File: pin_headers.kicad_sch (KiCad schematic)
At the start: 0 parts

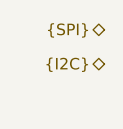
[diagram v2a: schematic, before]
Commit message: Follow DC-DC typical application
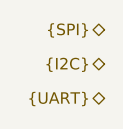
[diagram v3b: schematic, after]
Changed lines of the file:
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@@
 		(rev "1.0")
+	)
+	(hierarchical_label "{UART}"
+		(shape bidirectional)
+		(at 109.22 88.9 180)
+		(effects
+			(font
+				(size 1.27 1.27)
+			)
+			(justify right)
+		)
 	)
 	(hierarchical_label "{SPI}"

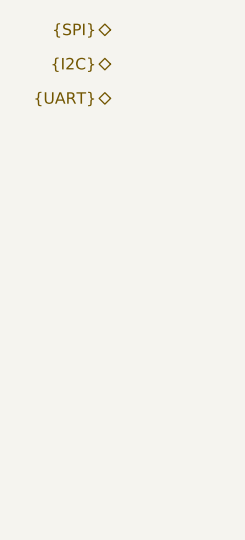
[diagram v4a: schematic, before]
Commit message: Reset PCB and lock mounting holes
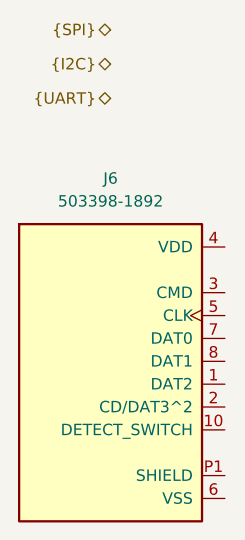
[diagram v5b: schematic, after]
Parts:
- added J6: 503398-1892, Tumbler2:MOLEX_503398-1892, symbol Tumbler2:503398-1892
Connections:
- new net: J6.P1 (SHIELD), J6.P2 (SHIELD), J6.P3 (SHIELD), J6.P4 (SHIELD)
- new net VSS: J6.6 (VSS), J6.9 (VSS)
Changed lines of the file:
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@@
+		)
+	)
+	(symbol
+		(lib_id "Tumbler2:503398-1892")
+		(at 109.22 119.38 0)
+		(unit 1)
+		(exclude_from_sim no)
+		(in_bom yes)
+		(on_board yes)
+		(dnp no)
+		(fields_autoplaced yes)
+		(property "Reference" "J6"
+			(at 109.22 97.79 0)
+			(effects
+				(font
+					(size 1.27 1.27)
+				)
+			)
+		)
+		(property "Value" "503398-1892"
+			(at 109.22 100.33 0)
+			(effects
+				(font
+					(size 1.27 1.27)
+				)
+			)
+		)
+		(property "Footprint" "Tumbler2:MOLEX_503398-1892"
+			(at 109.22 119.38 0)
+			(effects
+				(font
+					(size 1.27 1.27)
+				)
+				(justify bottom)
+				(hide yes)
+			)
+		)
+		(property "Datasheet" "https://www.molex.com/en-us/products/part-detail/5033981892?display=pdf"
+			(at 109.22 119.38 0)
+			(effects
+				(font
+					(size 1.27 1.27)
+				)
+				(hide yes)
+			)
+		)
+		(property "Description" "Micro SD card (TF card) Connector and Ejector Push-Push Surface Mount"
+			(at 109.22 119.38 0)
+			(effects
+				(font
+					(size 1.27 1.27)
+				)
+				(hide yes)
+			)
+		)
+		(property "LSCS Part Nr." "C428492"
+			(at 109.22 119.38 0)
+			(effects
+				(font
+					(size 1.27 1.27)
+				)
+				(hide yes)
+			)
+		)
+		(property "SnapEDA_Link" "https://www.snapeda.com/parts/503398-1892/Molex/view-part/?ref=snap"
+			(at 109.22 119.38 0)
+			(effects
+				(font
+					(size 1.27 1.27)
+				)
+				(justify bottom)
+				(hide yes)
+			)
+		)
+		(pin "4"
+		)
+		(pin "3"
+		)
+		(pin "5"
+		)
+		(pin "7"
+		)
+		(pin "8"
+		)
+		(pin "P2"
+		)
+		(pin "P4"
+		)
+		(pin "9"
+		)
+		(pin "P3"
+		)
+		(pin "10"
+		)
+		(pin "P1"
+		)
+		(pin "6"
+		)
+		(pin "1"
+		)
+		(pin "2"
+		)
+		(instances
+			(project ""
+				(path "/f3fd8d79-9d35-4c04-811e-2697a2740958/13a39940-d4ea-453b-93b0-cf8a2a454837"
+					(reference "J6")
+					(unit 1)
+				)
+			)
 		)
 	)

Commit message: Update LCSC symbol field
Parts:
- J6: LCSC Part (none) -> C428492; LSCS Part Nr. C428492 -> (none)
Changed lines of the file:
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@@
-			)
-		)
-		(property "LSCS Part Nr." "C428492"
-			(at 109.22 119.38 0)
-			(effects
-				(font
-					(size 1.27 1.27)
-				)
-				(hide yes)
 			)
 		)
@@
 				(hide yes)
 			)
+		)
+		(property "LCSC Part" "C428492"
+			(at 109.22 119.38 0)
+			(effects
+				(font
+					(size 1.27 1.27)
+				)
+				(hide yes)
+			)

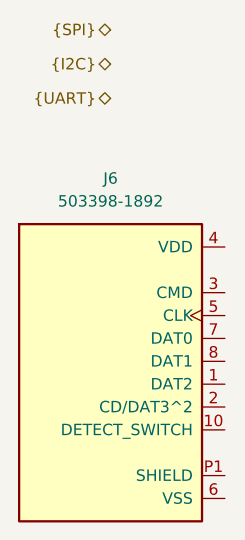
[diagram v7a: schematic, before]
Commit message: Undo component replacement
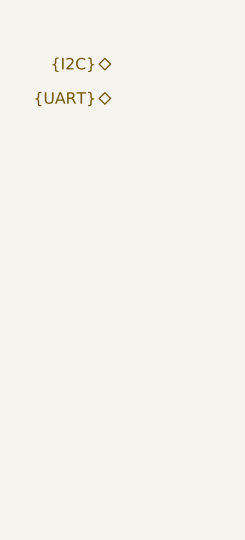
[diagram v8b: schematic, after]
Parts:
- removed J6: 503398-1892, Tumbler2:MOLEX_503398-1892, symbol Tumbler2:503398-1892
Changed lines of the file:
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@@
-		)
-	)
-	(hierarchical_label "{SPI}"
-		(shape bidirectional)
-		(at 109.22 81.28 180)
-		(effects
-			(font
-				(size 1.27 1.27)
-			)
-			(justify right)
 		)
 	)
@@
 		)
 	)
-	(symbol
-		(lib_id "Tumbler2:503398-1892")
-		(at 109.22 119.38 0)
-		(unit 1)
-		(exclude_from_sim no)
-		(in_bom yes)
-		(on_board yes)
-		(dnp no)
-		(fields_autoplaced yes)
-		(property "Reference" "J6"
-			(at 109.22 97.79 0)
-			(effects
-				(font
-					(size 1.27 1.27)
-				)
-			)
-		)
-		(property "Value" "503398-1892"
-			(at 109.22 100.33 0)
-			(effects
-				(font
-					(size 1.27 1.27)
-				)
-			)
-		)
-		(property "Footprint" "Tumbler2:MOLEX_503398-1892"
-			(at 109.22 119.38 0)
-			(effects
-				(font
-					(size 1.27 1.27)
-				)
-				(justify bottom)
-				(hide yes)
-			)
-		)
-		(property "Datasheet" "https://www.molex.com/en-us/products/part-detail/5033981892?display=pdf"
-			(at 109.22 119.38 0)
-			(effects
-				(font
-					(size 1.27 1.27)
-				)
-				(hide yes)
-			)
-		)
-		(property "Description" "Micro SD card (TF card) Connector and Ejector Push-Push Surface Mount"
-			(at 109.22 119.38 0)
-			(effects
-				(font
-					(size 1.27 1.27)
-				)
-				(hide yes)
-			)
-		)
-		(property "SnapEDA_Link" "https://www.snapeda.com/parts/503398-1892/Molex/view-part/?ref=snap"
-			(at 109.22 119.38 0)
-			(effects
-				(font
-					(size 1.27 1.27)
-				)
-				(justify bottom)
-				(hide yes)
-			)
-		)
-		(property "LCSC Part" "C428492"
-			(at 109.22 119.38 0)
-			(effects
-				(font
-					(size 1.27 1.27)
-				)
-				(hide yes)
-			)
-		)
-		(pin "4"
-		)
-		(pin "3"
-		)
-		(pin "5"
-		)
-		(pin "7"
-		)
-		(pin "8"
-		)
-		(pin "P2"
-		)
-		(pin "P4"
-		)
-		(pin "9"
-		)
-		(pin "P3"
-		)
-		(pin "10"
-		)
-		(pin "P1"
-		)
-		(pin "6"
-		)
-		(pin "1"
-		)
-		(pin "2"
-		)
-		(instances
-			(project ""
-				(path "/f3fd8d79-9d35-4c04-811e-2697a2740958/13a39940-d4ea-453b-93b0-cf8a2a454837"
-					(reference "J6")
-					(unit 1)
-				)
-			)
-		)
-	)
